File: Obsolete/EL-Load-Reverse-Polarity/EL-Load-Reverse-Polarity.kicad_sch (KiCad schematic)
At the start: 48 parts, among them J1 Conn_01x02_Socket, J2 Conn_01x02_Socket, J3 Conn_01x10_Male, Q1 AOSP66923, Q2 IRFP250M, U1 MCP6V51, U5 MCP6V51

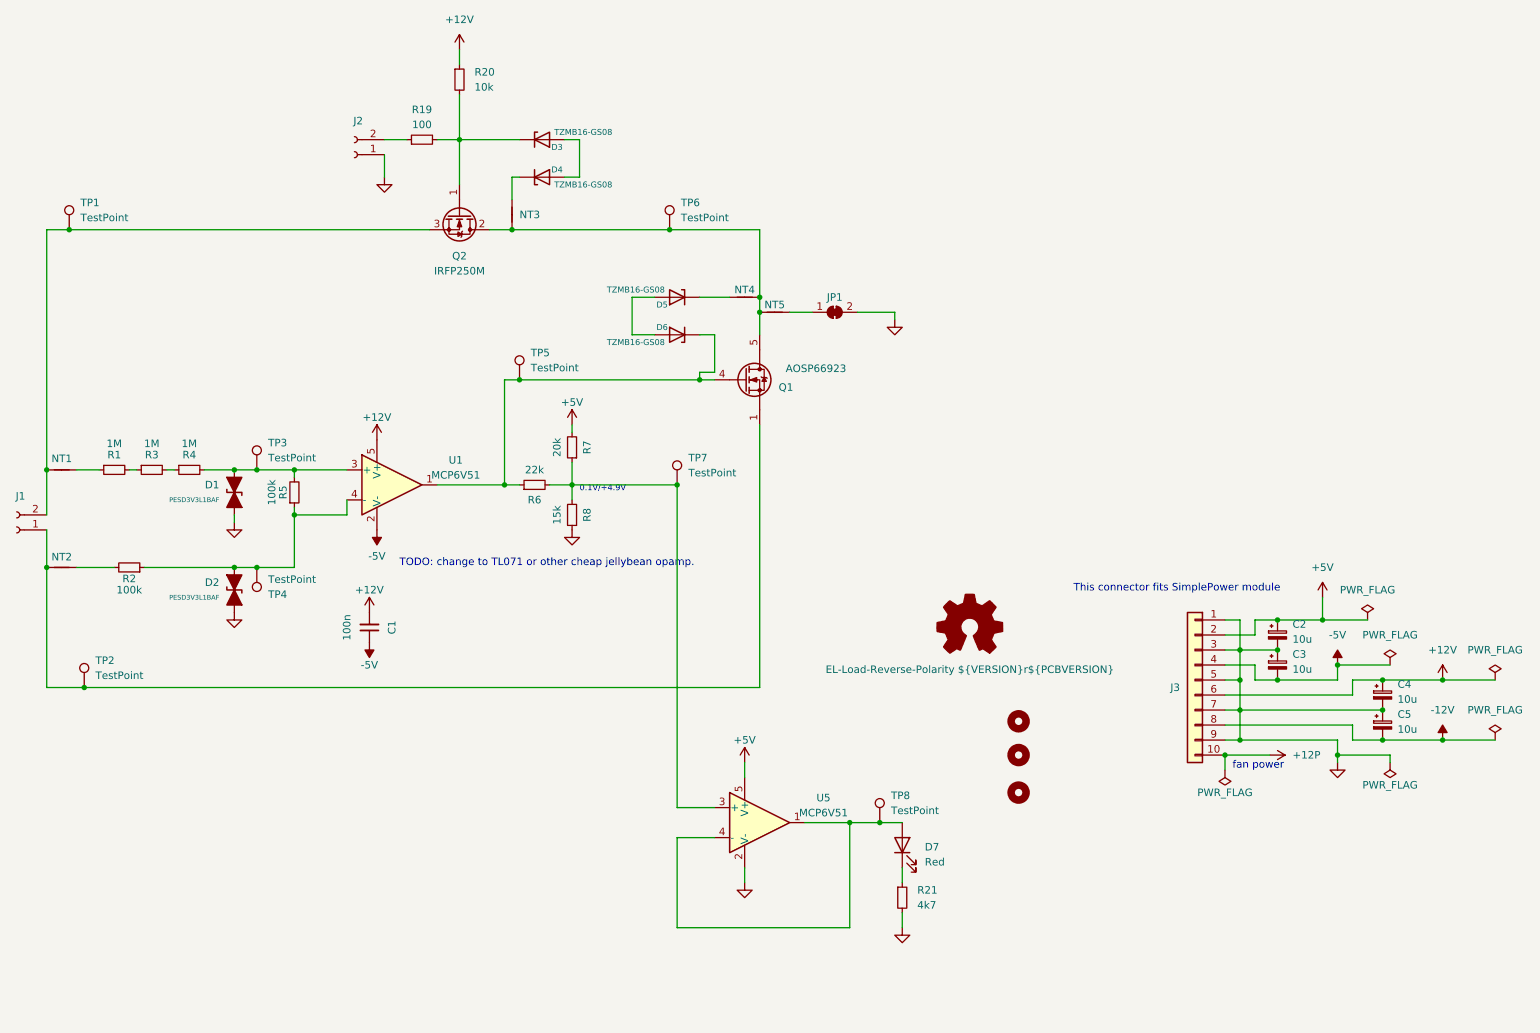
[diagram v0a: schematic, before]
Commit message: New reverse polarity test schema & PCB.
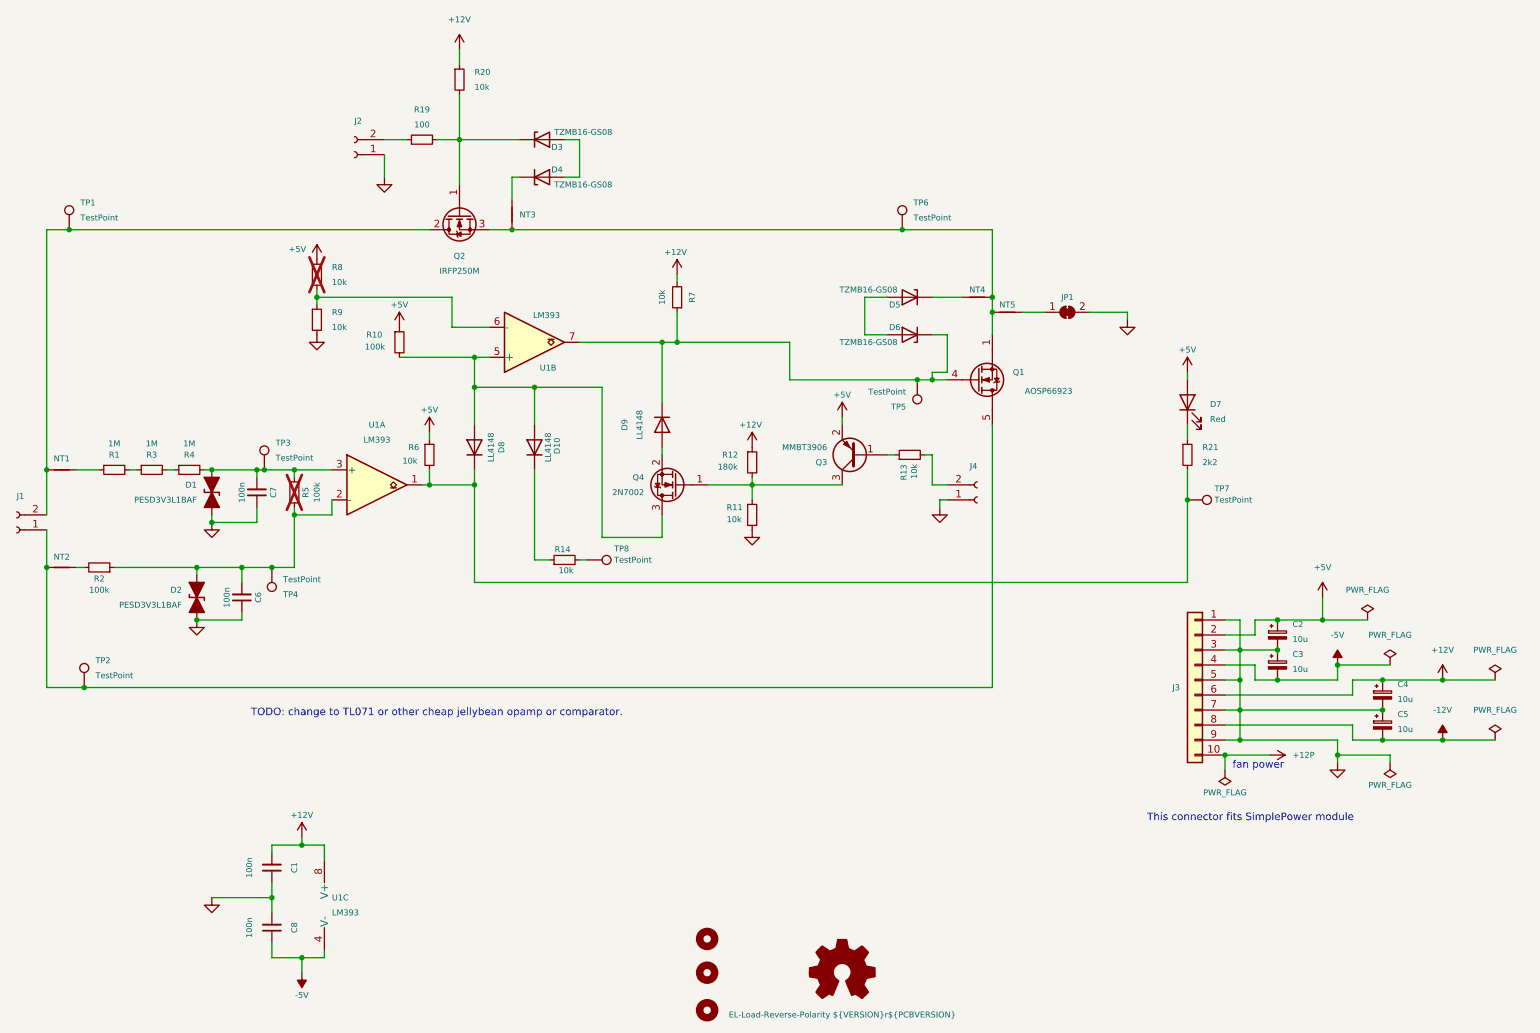
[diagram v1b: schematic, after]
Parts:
- removed U1, U5: MCP6V51, Package_TO_SOT_SMD:SOT-23-5, symbol EL-Load:MCP6V51/LTC2050HV
- added C6, C7, C8: 100n, Capacitor_SMD:C_0805_2012Metric, symbol Device:C_Small
- added D10, D8, D9: LL4148, Diode_SMD:D_MiniMELF, symbol Diode:LL4148
- added J4: Conn_01x02_Socket, Connector_Phoenix_MC:PhoenixContact_MCV_1,5_2-G-3.81_1x02_P3.81mm_Vertical, symbol Connector:Conn_01x02_Socket
- added Q3: MMBT3906, Package_TO_SOT_SMD:SOT-23, symbol Transistor_BJT:MMBT3906
- added Q4: 2N7002, Package_TO_SOT_SMD:SOT-23, symbol Transistor_FET:2N7002
- added R10: 100k, Resistor_SMD:R_0805_2012Metric, symbol Device:R_Small
- added R11, R13, R14, R9: 10k, Resistor_SMD:R_0805_2012Metric, symbol Device:R_Small
- added R12: 180k, Resistor_SMD:R_0805_2012Metric, symbol Device:R_Small
- added U1: LM393, Package_SO:SOIC-8_3.9x4.9mm_P1.27mm, symbol Comparator:LM393
- C2, C3, C4, C5: footprint Capacitor_SMD:C_0805_2012Metric_Pad1.18x1.45mm_HandSolder -> Capacitor_SMD:C_0805_2012Metric
- R21: value 4k7 -> 2k2; Part Name R_4.7kΩ_0805_1% -> R_2.2kΩ_0805_1%
- R5: now not fitted; now left out of the parts list
- R6: value 22k -> 10k; Part Name R_22.0kΩ_0805_1% -> R_10.0kΩ_0805_1%
- R7: value 20k -> 10k; Part Name R_20.0kΩ_0805_1% -> R_10.0kΩ_0805_1%
- R8: value 15k -> 10k; Part Name R_15.0kΩ_0805_1% -> R_10.0kΩ_0805_1%; now not fitted
- TP1, TP2, TP3, TP4, TP5, TP6, TP7, TP8: now left out of the parts list
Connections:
- net +12V: now also R7.2, R12.1, U1.8 (V+)
- net +5V: now also D7.2 (A), R6.1, R8.1, Q3.2 (E), R10.1; no longer R7.2
- net -5V: now also C8.1, U1.4 (V-); no longer C1.1
- net GND: now also C1.1, C6.1, C7.1, C8.2, J4.1 (Pin_1), R11.2, R9.2; no longer R21.2, R8.1
- net at D6.1 (K), Q1.4 (G), TP5.1: now also R7.1, D9.1 (K), U1.7; no longer R6.1
- net at J1.2 (Pin_2), NT1.2, TP1.1: now also Q2.2 (D); no longer Q2.3 (S)
- net at J1.1 (Pin_1), NT2.1, TP2.1: now also Q1.5 (D), Q1.6 (D), Q1.7 (D), Q1.8 (D); no longer Q1.1 (S), Q1.2 (S), Q1.3 (S)
- net at D2.2 (A2), R2.1, R5.1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: now also C6.2, U1.2 (-)
- net at D1.2 (A2), R4.2, R5.2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: now also C7.2, U1.3 (+)
- net at R6.2, TP7.1: now also R21.2, D8.1 (K), U1.1; no longer R7.1, R8.2
- net at TP8.1: now also R14.2; no longer D7.2 (A)
- new net: D10.2 (A), D8.2 (A), Q4.3 (D), R10.2, U1.5 (+)
- new net: R8.2, R9.1, U1.6 (-)
- new net: D10.1 (K), R14.1
- new net: Q3.3 (C), Q4.1 (G), R11.1, R12.2
- new net: NT3.2, NT4.1, NT5.2, Q1.1 (S), Q1.2 (S), Q1.3 (S), Q2.3 (S), TP6.1
- new net: D9.2 (A), Q4.2 (S)
- new net: Q3.1 (B), R13.1
- new net: J4.2 (Pin_2), R13.2
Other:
- note added: "TODO: change to TL071 or other cheap jellybean opamp or comparator."
- note removed: "0.1V/+4.9V"
- note removed: "TODO: change to TL071 or other cheap jellybean opamp."
- moved on the sheet: C1, D1, D2, D5, D6, D7, JP1, NT4, NT5, Q1, Q2, R2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
